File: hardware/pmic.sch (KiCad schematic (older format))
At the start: 72 parts, among them U601 TPS8208x, U602 TPS8208x, U603 TPSM84424, U604 TPSM84424, U605 TPS8208x, U606 TPS8208x, U607 TPS8208x, U608 TPS3808G01, U609 MCP1700-2502E_SOT23

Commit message: Routed extra GPIO Solder Pads, reannotated the whole schematic to make it consistent.
Power Distribution routing WIP
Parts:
- renumbered C601 to C501, C602 to C502, C603 to C503, C604 to C504, C605 to C505, C606 to C506, C607 to C507, C608 to C508, C609 to C509, C610 to C510, C611 to C511, C612 to C512, C613 to C513, C614 to C514, C615 to C515, C616 to C516, C617 to C517, C618 to C518, C619 to C519, C620 to C520, C621 to C521, C622 to C522, R601 to R501, R602 to R502, R603 to R503, R604 to R504, R605 to R505, R606 to R506, R607 to R507, R608 to R508, R609 to R509, R610 to R510, R611 to R511, R612 to R512, R613 to R513, R614 to R514, R615 to R515, R616 to R516, R617 to R517, R618 to R518, R619 to R519, R628 to R520, R620 to R521, R621 to R522, R622 to R523, R623 to R524, R624 to R525, R625 to R526, R626 to R527, R627 to R528, U601 to U501, U602 to U502, U603 to U503, U604 to U504, U605 to U505, U606 to U506, U607 to U507, U608 to U508, U609 to U509

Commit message: general routing mainly power distribution, fixed some footprints
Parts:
- U509: footprint TO_SOT_Packages_SMD:SOT-23 -> Package_TO_SOT_SMD:SOT-23
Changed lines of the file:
@@
 F 0 "U509" H 14650 6050 50  0000 C CNN
 F 1 "MCP1700-2502E_SOT23" H 14050 6450 50  0000 L CNN
-F 2 "TO_SOT_Packages_SMD:SOT-23" H 14500 6525 50  0001 C CNN
+F 2 "Package_TO_SOT_SMD:SOT-23" H 14500 6525 50  0001 C CNN
 F 3 "http://www.microchip.com/mymicrochip/filehandler.aspx?ddocname=en011779" H 14500 6300 50  0001 C CNN
 F 4 "Microchip Technology" H 14500 6300 60  0001 C CNN "MFG Name"

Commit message: WIP: general routing.
I got the advice to use at least 125 µm isolation between copper layers in the stackup. This will create the need to change the top/bottom impedance matched traces. This is a TODO
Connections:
- net labels added: AGND_1V, AGND_5V
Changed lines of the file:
@@
 	9100 2400 10000 2400
 NoConn ~ 9500 2000
+Text Label 5200 2700 0    50   ~ 0
+AGND_5V
+Text Label 5250 5100 0    50   ~ 0
+AGND_1V
 $EndSCHEMATC

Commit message: First Version without any Net not routed.
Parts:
- added TP514: Test_Point, footprints:TestPoint_SMD_0.5mm, symbol Connector:Test_Point
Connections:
- net labels added: SYS_PG
- net labels removed: PS_POR_B
- wire segments 399 -> 400
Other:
- note added: "PS_POR"
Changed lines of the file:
@@
 	1    0    0    -1
 $EndComp
-Text HLabel 12850 1800 2    60   Output ~ 0
-PS_POR_B
 $Comp
 L power:+5V #PWR0509
@@
 P 14500 6300
 F 0 "U509" H 14650 6050 50  0000 C CNN
-F 1 "MCP1700-2502E_SOT23" H 14050 6450 50  0000 L CNN
+F 1 "MCP1700-2502E_SOT23" H 14050 6850 50  0000 L CNN
 F 2 "Package_TO_SOT_SMD:SOT-23" H 14500 6525 50  0001 C CNN
 F 3 "http://www.microchip.com/mymicrochip/filehandler.aspx?ddocname=en011779" H 14500 6300 50  0001 C CNN
@@
 U 1 1 5AFAD2F1
 P 14100 6500
-F 0 "C521" H 14110 6570 50  0000 L CNN
-F 1 "1 µF 6.3 V" H 14110 6420 50  0000 L CNN
+F 0 "C521" H 13900 6600 50  0000 L CNN
+F 1 "1 µF 6.3 V" H 13650 6400 50  0000 L CNN
 F 2 "Capacitor_SMD:C_0402_1005Metric" H 14100 6500 50  0001 C CNN
 F 3 "http://search.murata.co.jp/Ceramy/image/img/A01X/G101/ENG/GRM152R60J105ME15-01.pdf" H 14100 6500 50  0001 C CNN
@@
 	14900 6300 15000 6300
 Wire Wire Line
-	14100 6300 14200 6300
+	14100 6300 14150 6300
 Connection ~ 6650 4900
 Wire Wire Line
@@
 U 1 1 5BA692AB
 P 14800 6300
-F 0 "TP513" H 14858 6420 50  0000 L CNN
-F 1 "Test_Point" H 14858 6329 50  0000 L CNN
+F 0 "TP513" V 14800 6500 50  0000 L CNN
+F 1 "Test_Point" H 14858 6329 50  0001 L CNN
 F 2 "footprints:TestPoint_SMD_0.5mm" H 15000 6300 50  0001 C CNN
 F 3 "~" H 15000 6300 50  0001 C CNN
@@
 Text Label 5250 5100 0    50   ~ 0
 AGND_1V
+$Comp
+L Connector:Test_Point TP514
+U 1 1 5B6308AF
+P 14150 6300
+F 0 "TP514" V 14150 6500 50  0000 L CNN
+F 1 "Test_Point" H 14208 6329 50  0001 L CNN
+F 2 "footprints:TestPoint_SMD_0.5mm" H 14350 6300 50  0001 C CNN
+F 3 "~" H 14350 6300 50  0001 C CNN
+F 4 "1" H 14150 6300 50  0001 C CNN "Populated"
+F 5 "SPEC" H 14150 6300 50  0001 C CNN "Source"
+F 6 "1" H 14150 6300 50  0001 C CNN "Populate for SBGA485(Z-7030)"
+F 7 "1" H 14150 6300 50  0001 C CNN "Populate for CLG484(Z-7012s/Z-7015)"
+	1    14150 6300
+	1    0    0    -1
+$EndComp
+Connection ~ 14150 6300
+Wire Wire Line
+	14150 6300 14200 6300
+Text GLabel 12850 1800 2    50   Output ~ 0
+SYS_PG
+Text Notes 12850 1950 0    50   ~ 0
+PS_POR
 $EndSCHEMATC

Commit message: Add sym-lib-table and fp-lib-table, fixes for KiCad 5
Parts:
- TP501, TP502, TP503, TP504, TP505, TP506, TP507, TP508, TP509, TP510, TP511, TP512, TP513, TP514: symbol Connector:Test_Point -> Connector:TestPoint
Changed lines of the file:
@@
 For 300 ms Delay a 40 kΩ to 200 kΩ\nResistor must be used!
 $Comp
-L Connector:Test_Point TP501
+L Connector:TestPoint TP501
 U 1 1 5BA66623
 P 3150 1400
@@
 Connection ~ 3150 1400
 $Comp
-L Connector:Test_Point TP507
+L Connector:TestPoint TP507
 U 1 1 5BA67D98
 P 6900 1400
@@
 	6900 1400 7150 1400
 $Comp
-L Connector:Test_Point TP506
+L Connector:TestPoint TP506
 U 1 1 5BA68001
 P 6850 3800
@@
 	6850 3800 7150 3800
 $Comp
-L Connector:Test_Point TP509
+L Connector:TestPoint TP509
 U 1 1 5BA68399
 P 11100 3800
@@
 	11100 3800 11050 3800
 $Comp
-L Connector:Test_Point TP510
+L Connector:TestPoint TP510
 U 1 1 5BA6850D
 P 11150 6450
@@
 	11150 6450 11050 6450
 $Comp
-L Connector:Test_Point TP505
+L Connector:TestPoint TP505
 U 1 1 5BA68943
 P 6600 6450
@@
 	6600 6450 7150 6450
 $Comp
-L Connector:Test_Point TP504
+L Connector:TestPoint TP504
 U 1 1 5BA68D28
 P 6550 8750
@@
 	6550 8750 7150 8750
 $Comp
-L Connector:Test_Point TP511
+L Connector:TestPoint TP511
 U 1 1 5BA68F86
 P 11150 8750
@@
 	11150 8750 11050 8750
 $Comp
-L Connector:Test_Point TP513
+L Connector:TestPoint TP513
 U 1 1 5BA692AB
 P 14800 6300
@@
 Connection ~ 14800 6300
 $Comp
-L Connector:Test_Point TP512
+L Connector:TestPoint TP512
 U 1 1 5BA69713
 P 11900 1800
@@
 	11900 1800 12100 1800
 $Comp
-L Connector:Test_Point TP503
+L Connector:TestPoint TP503
 U 1 1 5BA69BF2
 P 6400 4900
@@
 	6400 4900 6650 4900
 $Comp
-L Connector:Test_Point TP508
+L Connector:TestPoint TP508
 U 1 1 5BA69F8C
 P 9900 5800
@@
 	9900 5800 8050 5800
 $Comp
-L Connector:Test_Point TP502
+L Connector:TestPoint TP502
 U 1 1 5BA6AB30
 P 6350 7650
@@
 AGND_1V
 $Comp
-L Connector:Test_Point TP514
+L Connector:TestPoint TP514
 U 1 1 5B6308AF
 P 14150 6300

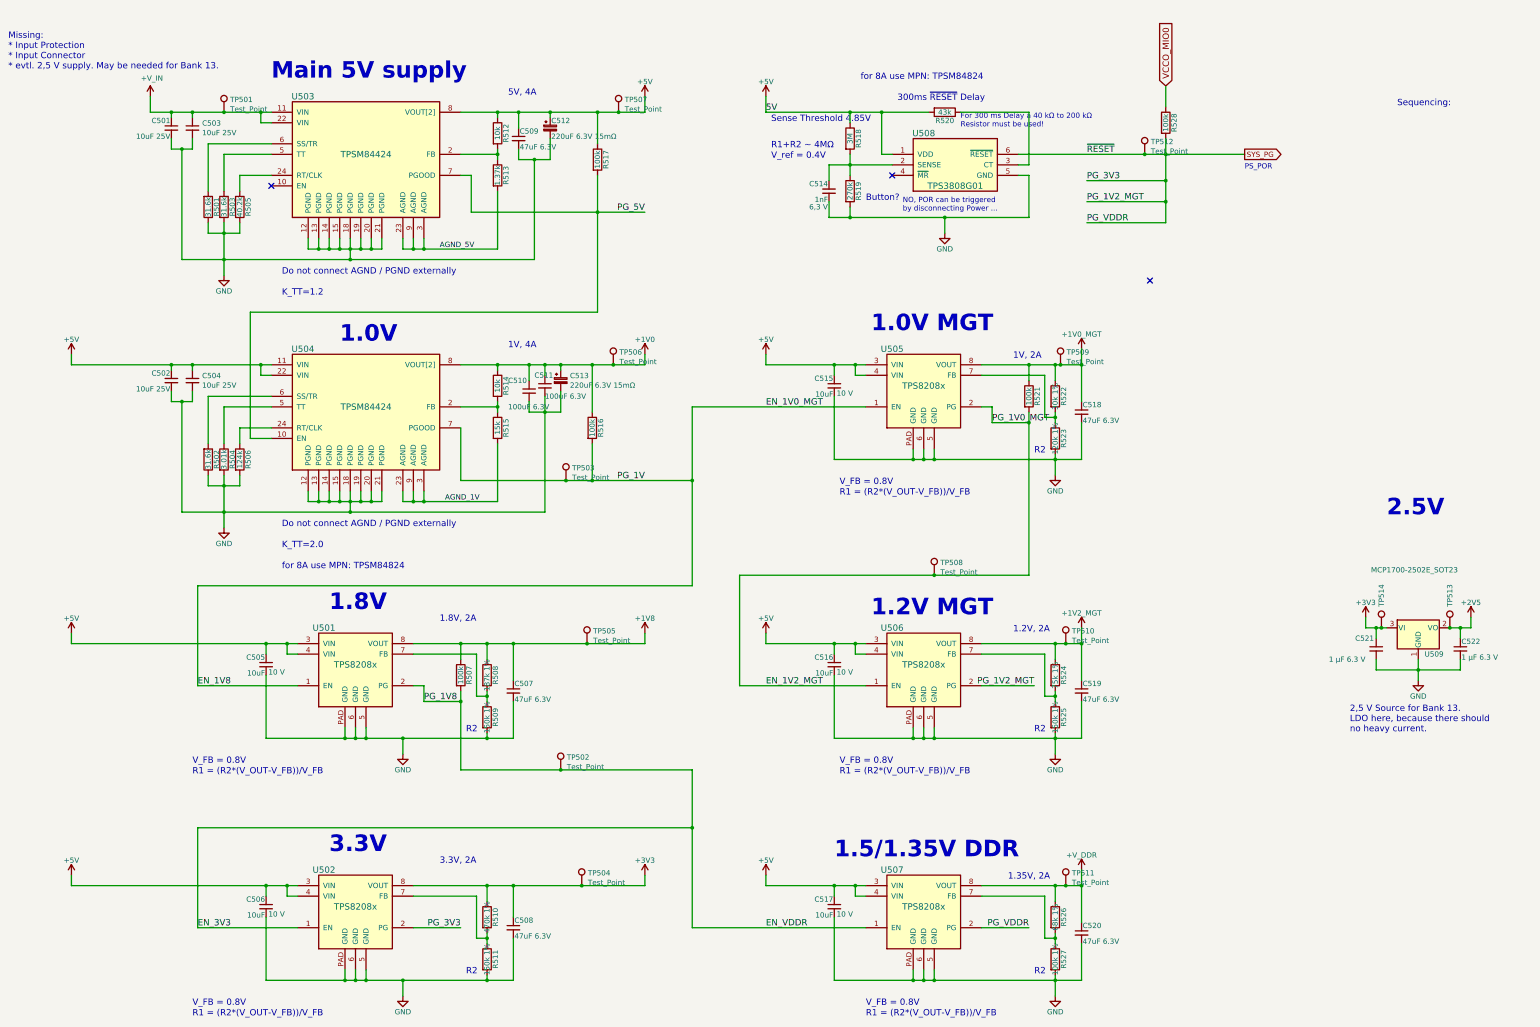
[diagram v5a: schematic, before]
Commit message: Added Step Models, fixed some footprints(e.g. added solderpaste), cleaned up a bit
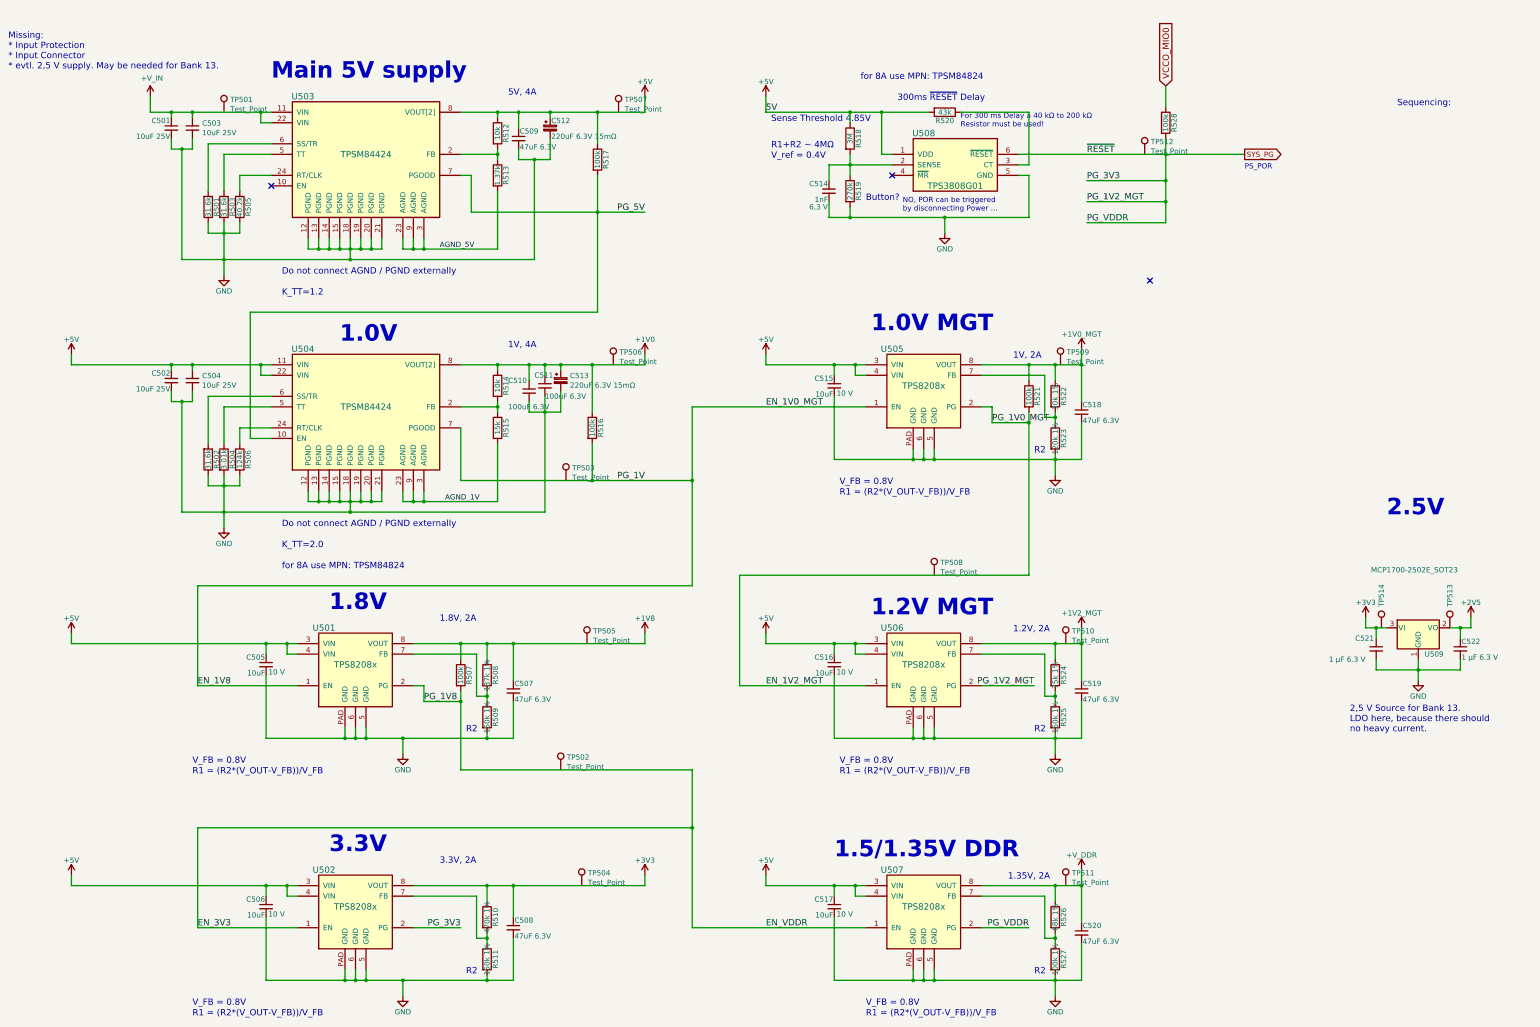
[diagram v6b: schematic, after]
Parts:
- C512, C513: footprint footprints:C7343-31_KEMET-D_10.22x5.6mm -> Capacitor_Tantalum_SMD:CP_EIA-7343-31_Kemet-D
- U501, U502, U505, U506, U507: footprint footprints:TI_MicroSiP_2.9x3.1mm -> footprints:Texas_MicroSiP_2.9x3.1mm
- U503, U504: footprint footprints:TI_QFM-24_MOL0024A -> footprints:Texas_QFM-24_MOL0024A
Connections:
- net +1V0: no longer TP506.1
- net +1V0_MGT: no longer TP509.1
- net +1V2_MGT: no longer TP510.1
- net +1V8: no longer TP505.1
- net +3V3: no longer TP504.1, TP514.1
- net +5V: no longer TP507.1
- net +V_DDR: no longer TP511.1
- net +V_IN: no longer TP501.1
- net EN_1V0_MGT: no longer TP503.1
- net EN_1V2_MGT: no longer TP508.1
- net EN_3V3: no longer TP502.1
- net SYS_PG: no longer TP512.1
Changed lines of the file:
@@
 EESchema Schematic File Version 4
 LIBS:zynq_board-cache
-EELAYER 26 0
+EELAYER 29 0
 EELAYER END
 $Descr A3 16535 11693
@@
 F 0 "U503" H 3900 2550 60  0000 C CNN
 F 1 "TPSM84424" H 4500 2000 60  0000 C CNN
-F 2 "footprints:TI_QFM-24_MOL0024A" H 4350 1800 60  0001 C CNN
+F 2 "footprints:Texas_QFM-24_MOL0024A" H 4350 1800 60  0001 C CNN
 F 3 "http://www.ti.com/lit/ds/symlink/tpsm84424.pdf" H 4350 1800 60  0001 C CNN
 F 4 "Texas Instruments" H 4500 1900 60  0001 C CNN "MFG Name"
@@
 F 0 "C512" H 6260 1620 50  0000 L CNN
 F 1 "220uF 6.3V 15mΩ" H 6260 1470 50  0000 L CNN
-F 2 "footprints:C7343-31_KEMET-D_10.22x5.6mm" H 6250 1550 50  0001 C CNN
+F 2 "Capacitor_Tantalum_SMD:CP_EIA-7343-31_Kemet-D" H 6250 1550 50  0001 C CNN
 F 3 "https://search.kemet.com/component-edge/download/datasheet/T520D227M006ATE015.pdf" H 6250 1550 50  0001 C CNN
 F 4 "Kemet" H 6250 1550 60  0001 C CNN "MFG Name"
@@
 F 0 "U502" H 4100 9400 60  0000 C CNN
 F 1 "TPS8208x" H 4400 9050 60  0000 C CNN
-F 2 "footprints:TI_MicroSiP_2.9x3.1mm" H 4450 8900 60  0001 C CNN
+F 2 "footprints:Texas_MicroSiP_2.9x3.1mm" H 4450 8900 60  0001 C CNN
 F 3 "http://www.ti.com/lit/ds/symlink/tps82084.pdf" H 4450 8900 60  0001 C CNN
 F 4 "Texas Instruments" H 4400 9000 60  0001 C CNN "MFG Name"
@@
 F 0 "U501" H 4100 7100 60  0000 C CNN
 F 1 "TPS8208x" H 4400 6750 60  0000 C CNN
-F 2 "footprints:TI_MicroSiP_2.9x3.1mm" H 4450 6600 60  0001 C CNN
+F 2 "footprints:Texas_MicroSiP_2.9x3.1mm" H 4450 6600 60  0001 C CNN
 F 3 "http://www.ti.com/lit/ds/symlink/tps82084.pdf" H 4450 6600 60  0001 C CNN
 F 4 "Texas Instruments" H 4400 6700 60  0001 C CNN "MFG Name"
@@
 F 0 "U506" H 9500 7100 60  0000 C CNN
 F 1 "TPS8208x" H 9800 6750 60  0000 C CNN
-F 2 "footprints:TI_MicroSiP_2.9x3.1mm" H 9850 6600 60  0001 C CNN
+F 2 "footprints:Texas_MicroSiP_2.9x3.1mm" H 9850 6600 60  0001 C CNN
 F 3 "http://www.ti.com/lit/ds/symlink/tps82084.pdf" H 9850 6600 60  0001 C CNN
 F 4 "Texas Instruments" H 9800 6700 60  0001 C CNN "MFG Name"
@@
 F 0 "U507" H 9500 9400 60  0000 C CNN
 F 1 "TPS8208x" H 9800 9050 60  0000 C CNN
-F 2 "footprints:TI_MicroSiP_2.9x3.1mm" H 9850 8900 60  0001 C CNN
+F 2 "footprints:Texas_MicroSiP_2.9x3.1mm" H 9850 8900 60  0001 C CNN
 F 3 "http://www.ti.com/lit/ds/symlink/tps82084.pdf" H 9850 8900 60  0001 C CNN
 F 4 "Texas Instruments" H 9800 9000 60  0001 C CNN "MFG Name"
@@
 F 0 "U505" H 9500 4450 60  0000 C CNN
 F 1 "TPS8208x" H 9800 4100 60  0000 C CNN
-F 2 "footprints:TI_MicroSiP_2.9x3.1mm" H 9850 3950 60  0001 C CNN
+F 2 "footprints:Texas_MicroSiP_2.9x3.1mm" H 9850 3950 60  0001 C CNN
 F 3 "http://www.ti.com/lit/ds/symlink/tps82084.pdf" H 9850 3950 60  0001 C CNN
 F 4 "Texas Instruments" H 9800 4050 60  0001 C CNN "MFG Name"
@@
 F 0 "U504" H 3900 4950 60  0000 C CNN
 F 1 "TPSM84424" H 4500 4400 60  0000 C CNN
-F 2 "footprints:TI_QFM-24_MOL0024A" H 4350 4200 60  0001 C CNN
+F 2 "footprints:Texas_QFM-24_MOL0024A" H 4350 4200 60  0001 C CNN
 F 3 "http://www.ti.com/lit/ds/symlink/tpsm84424.pdf" H 4350 4200 60  0001 C CNN
 F 4 "Texas Instruments" H 4500 4300 60  0001 C CNN "MFG Name"
@@
 F 0 "C513" H 6438 3996 50  0000 L CNN
 F 1 "220uF 6.3V 15mΩ" H 6438 3905 50  0000 L CNN
-F 2 "footprints:C7343-31_KEMET-D_10.22x5.6mm" H 6350 3950 50  0001 C CNN
+F 2 "Capacitor_Tantalum_SMD:CP_EIA-7343-31_Kemet-D" H 6350 3950 50  0001 C CNN
 F 3 "https://search.kemet.com/component-edge/download/datasheet/T520D227M006ATE015.pdf" H 6350 3950 50  0001 C CNN
 F 4 "Kemet" H 6350 3950 60  0001 C CNN "MFG Name"
@@
 	6350 4250 6350 4050
 Wire Wire Line
-	10700 1800 11900 1800
-Wire Wire Line
 	10700 2000 10800 2000
 Wire Wire Line
@@
 	5400 4400 5400 4900
 Wire Wire Line
-	5400 4900 6400 4900
-Wire Wire Line
 	7600 4200 7600 4900
 Wire Wire Line
@@
 Connection ~ 7600 4900
 Wire Wire Line
-	10800 5800 9900 5800
-Wire Wire Line
 	8050 5800 8050 6850
 Connection ~ 10800 4350
 Wire Wire Line
-	5400 7650 6350 7650
-Wire Wire Line
 	7600 7650 7600 8200
 Connection ~ 5400 7000
@@
 	7150 3800 7150 3700
 Wire Wire Line
-	11300 8750 11150 8750
-Wire Wire Line
-	11300 6450 11150 6450
-Wire Wire Line
-	11300 3800 11100 3800
-Wire Wire Line
 	4250 5000 4250 5100
 Wire Wire Line
@@
 	4950 2700 5050 2700
 Wire Wire Line
-	3500 1400 3150 1400
-Wire Wire Line
 	3150 2550 3300 2550
 Wire Wire Line
@@
 	5650 7350 5900 7350
 Wire Wire Line
-	5900 6450 6600 6450
-Wire Wire Line
 	5650 9650 5900 9650
 Wire Wire Line
-	5900 8750 6550 8750
-Wire Wire Line
 	9800 7350 9900 7350
 Wire Wire Line
@@
 	9100 1400 9400 1400
 Wire Wire Line
-	6700 1400 6900 1400
-Wire Wire Line
 	6700 2350 7150 2350
 Wire Wire Line
 	6700 2350 6700 3300
 Wire Wire Line
-	6650 3800 6850 3800
-Wire Wire Line
 	7600 4900 7600 5900
 Wire Wire Line
@@
 Wire Wire Line
 	14900 6300 15000 6300
-Wire Wire Line
-	14100 6300 14150 6300
 Connection ~ 6650 4900
 Wire Wire Line
@@
 	1    0    0    -1
 $EndComp
-Wire Wire Line
-	3150 1400 2850 1400
-Connection ~ 3150 1400
 $Comp
 L Connector:TestPoint TP507
@@
 	1    0    0    -1
 $EndComp
-Connection ~ 6900 1400
-Wire Wire Line
-	6900 1400 7150 1400
 $Comp
 L Connector:TestPoint TP506
@@
 	1    0    0    -1
 $EndComp
-Connection ~ 6850 3800
-Wire Wire Line
-	6850 3800 7150 3800
 $Comp
 L Connector:TestPoint TP509
@@
 	1    0    0    -1
 $EndComp
-Connection ~ 11100 3800
-Wire Wire Line
-	11100 3800 11050 3800
 $Comp
 L Connector:TestPoint TP510
@@
 	1    0    0    -1
 $EndComp
-Connection ~ 11150 6450
-Wire Wire Line
-	11150 6450 11050 6450
 $Comp
 L Connector:TestPoint TP505
@@
 	1    0    0    -1
 $EndComp
-Connection ~ 6600 6450
-Wire Wire Line
-	6600 6450 7150 6450
 $Comp
 L Connector:TestPoint TP504
@@
 	1    0    0    -1
 $EndComp
-Connection ~ 6550 8750
-Wire Wire Line
-	6550 8750 7150 8750
 $Comp
 L Connector:TestPoint TP511
@@
 	1    0    0    -1
 $EndComp
-Connection ~ 11150 8750
-Wire Wire Line
-	11150 8750 11050 8750
 $Comp
 L Connector:TestPoint TP513
@@
 	1    0    0    -1
 $EndComp
-Connection ~ 14800 6300
 $Comp
 L Connector:TestPoint TP512
@@
 	1    0    0    -1
 $EndComp
-Connection ~ 11900 1800
-Wire Wire Line
-	11900 1800 12100 1800
 $Comp
 L Connector:TestPoint TP503
@@
 	1    0    0    -1
 $EndComp
-Connection ~ 6400 4900
-Wire Wire Line
-	6400 4900 6650 4900
 $Comp
 L Connector:TestPoint TP508
@@
 	1    0    0    -1
 $EndComp
-Connection ~ 9900 5800
-Wire Wire Line
-	9900 5800 8050 5800
 $Comp
 L Connector:TestPoint TP502
@@
 	1    0    0    -1
 $EndComp
-Connection ~ 6350 7650
-Wire Wire Line
-	6350 7650 7600 7650
 Wire Wire Line
 	5400 3800 5750 3800
@@
 	1    0    0    -1
 $EndComp
-Connection ~ 14150 6300
-Wire Wire Line
-	14150 6300 14200 6300
 Text GLabel 12850 1800 2    50   Output ~ 0
 SYS_PG
 Text Notes 12850 1950 0    50   ~ 0
 PS_POR
+Wire Wire Line
+	10700 1800 12100 1800
+Wire Wire Line
+	5400 4900 6650 4900
+Wire Wire Line
+	8050 5800 10800 5800
+Wire Wire Line
+	5400 7650 7600 7650
+Wire Wire Line
+	11050 8750 11300 8750
+Wire Wire Line
+	11050 6450 11300 6450
+Wire Wire Line
+	11050 3800 11300 3800
+Wire Wire Line
+	2850 1400 3500 1400
+Wire Wire Line
+	5900 6450 7150 6450
+Wire Wire Line
+	5900 8750 7150 8750
+Wire Wire Line
+	6700 1400 7150 1400
+Wire Wire Line
+	6650 3800 7150 3800
+Wire Wire Line
+	14100 6300 14200 6300
 $EndSCHEMATC
